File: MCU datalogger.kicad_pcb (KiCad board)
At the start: 2 copper layers, 51 x 32.8 mm, 29 parts, among them J1 Conn_01x04_Pin, J2 Conn_01x04_Pin, J3 Conn_01x09_Pin, J4 Conn_02x03_Odd_Even, U1 24LC1025, U2 24LC1025, U3 ATMEGA328P-AU, U4 DS1337S_, Y1 32.768KHz, Y2 16MHz

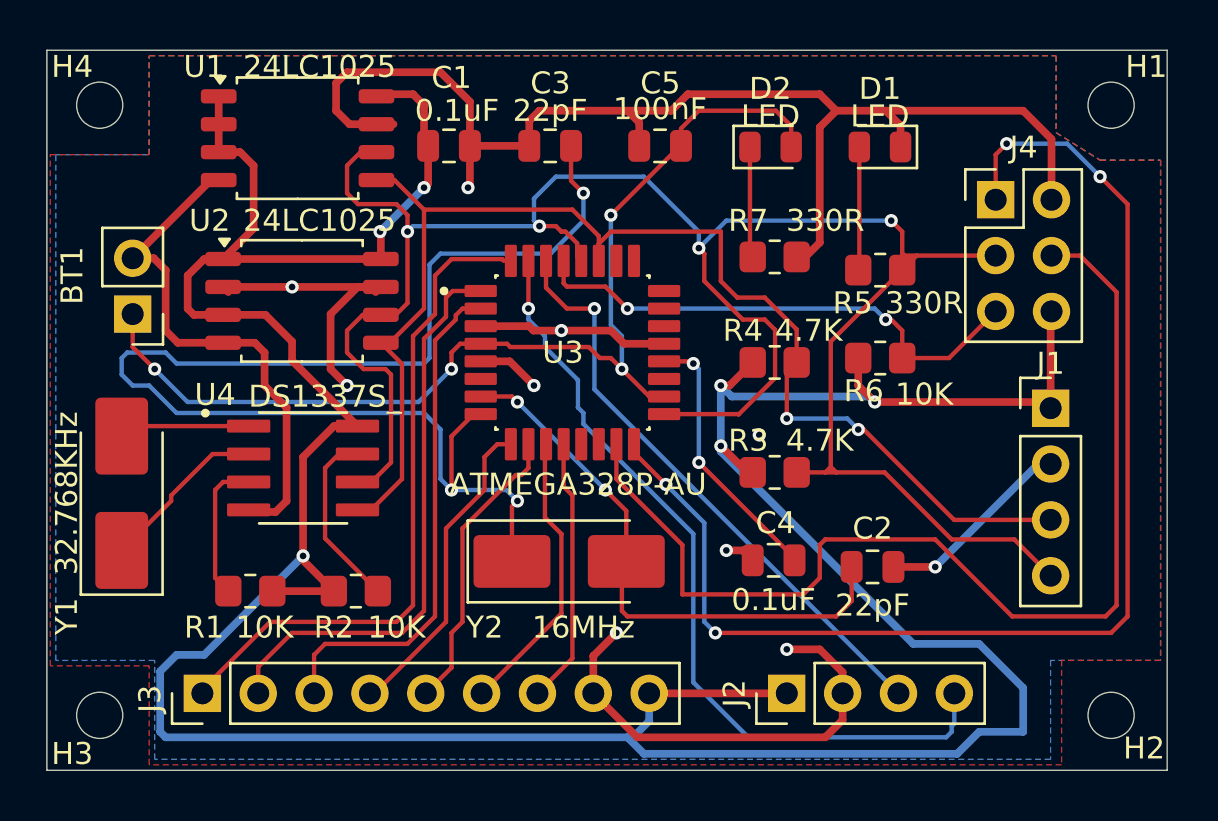
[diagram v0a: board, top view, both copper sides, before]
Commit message: Add copper layer
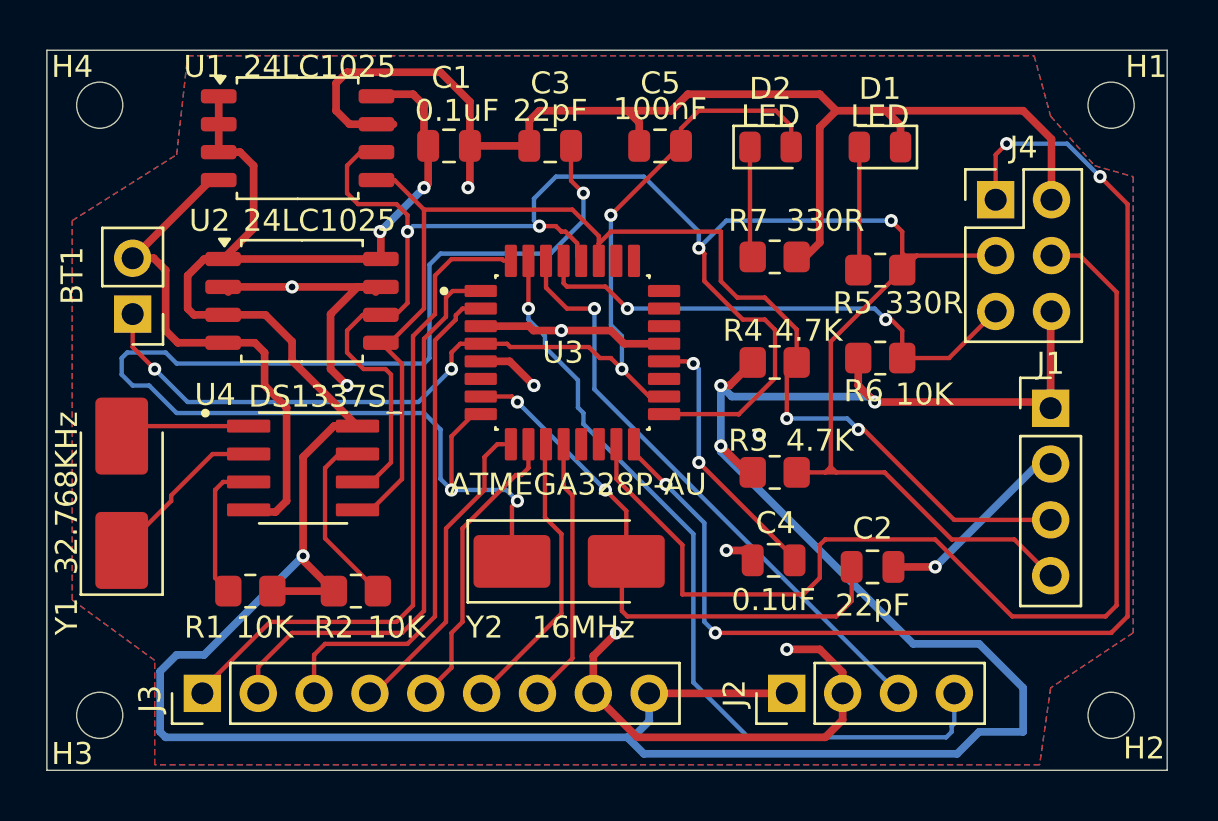
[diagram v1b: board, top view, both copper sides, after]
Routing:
- added copper zone on F.Cu, net GND
- removed copper zone on F.Cu, net /VCC
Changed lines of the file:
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@@
 	)
 	(zone
-		(net 3)
-		(net_name "/VCC")
-		(layer "F.Cu")
+		(net 2)
+		(net_name "GND")
+		(layers "F.Cu" "B.Cu")
 		(hatch edge 0.5)
 		(connect_pads
@@
 		(polygon
 			(pts
-				(xy 1987.25 2085.25) (xy 1987.25 2088.75) (xy 1989.25 2090) (xy 1992 2090) (xy 1992 2112.75) (xy 1987.5 2112.75)
-				(xy 1987.5 2117.5) (xy 1946 2117.5) (xy 1946 2113) (xy 1941.5 2113) (xy 1941.5 2089.75) (xy 1946 2089.75)
-				(xy 1946 2085.25)
+				(xy 1986.25 2085.25) (xy 1987 2088) (xy 1989 2090.25) (xy 1990.75 2090.75) (xy 1990.75 2111.5) (xy 1987 2114)
+				(xy 1986.5 2117.5) (xy 1946.25 2117.5) (xy 1946.25 2112.75) (xy 1942.5 2110) (xy 1942.5 2092.75)
+				(xy 1947.25 2089.75) (xy 1947.75 2085.25)
 			)
 		)
-	)
-	(zone
-		(net 2)
-		(net_name "GND")
-		(layer "B.Cu")
-		(hatch edge 0.5)
-		(priority 1)
-		(connect_pads
-			(clearance 0.5)
-		)
-		(min_thickness 0.25)
-		(filled_areas_thickness no)
-		(fill yes
-			(mode hatch)
-			(thermal_gap 0.5)
-			(thermal_bridge_width 0.5)
-			(hatch_thickness 1)
-			(hatch_gap 1.5)
-			(hatch_orientation 0)
-			(hatch_border_algorithm hatch_thickness)
-			(hatch_min_hole_area 0.3)
-		)
-		(polygon
-			(pts
-				(xy 1987.25 2085.25) (xy 1987.25 2088.75) (xy 1989.25 2090) (xy 1992 2090) (xy 1992 2112.75) (xy 1987 2112.75)
-				(xy 1987 2117.25) (xy 1946.25 2117.25) (xy 1946.25 2112.75) (xy 1941.75 2112.75) (xy 1941.75 2089.75)
-				(xy 1946 2089.75) (xy 1946 2085.25)
-			)
-		)
